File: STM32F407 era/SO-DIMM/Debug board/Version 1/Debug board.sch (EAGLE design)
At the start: 10 parts, among them J4 FTDI_DEVICE, X1 057-014-1, X2 BN35N61, X3 BN35N61, X4 BN35N61, X5 BN35N61, X6 BN35N61

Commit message: more work on debug board silkscreen
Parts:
- added J2, J3, J5, J6, J7: (no value), SparkFun-Connectors:BANANA_CONN
- R26: value 60 -> 120
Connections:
- net CANH renamed CAN_P
- net CANL renamed CAN_N
- net 12V: now also J5.1
- net 3.3V: now also J2.1
- net 5.0V: now also J3.1
- net GND: now also J6.1, J7.1
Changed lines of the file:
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@@
 <part name="GND7" library="supply1" deviceset="GND" device=""/>
 <part name="SW1" library="microbuilder" deviceset="SWITCH_DPDT" device=""/>
-<part name="R26" library="microbuilder" deviceset="RESISTOR" device="_0603" value="60"/>
+<part name="R26" library="microbuilder" deviceset="RESISTOR" device="_0603" value="120"/>
 <part name="X2" library="con-coax" deviceset="BN35N61" device=""/>
 <part name="X3" library="con-coax" deviceset="BN35N61" device=""/>
@@
 <part name="X5" library="con-coax" deviceset="BN35N61" device=""/>
 <part name="X6" library="con-coax" deviceset="BN35N61" device=""/>
+<part name="J2" library="SparkFun-Connectors" deviceset="BANANA_CONN" device=""/>
+<part name="J3" library="SparkFun-Connectors" deviceset="BANANA_CONN" device=""/>
+<part name="J5" library="SparkFun-Connectors" deviceset="BANANA_CONN" device=""/>
+<part name="J6" library="SparkFun-Connectors" deviceset="BANANA_CONN" device=""/>
+<part name="U$1" library="microbuilder" deviceset="3.3V" device=""/>
+<part name="U$2" library="microbuilder" deviceset="5.0V" device=""/>
+<part name="U$3" library="microbuilder" deviceset="12V" device=""/>
+<part name="GND9" library="supply1" deviceset="GND" device=""/>
+<part name="J7" library="SparkFun-Connectors" deviceset="BANANA_CONN" device=""/>
 </parts>
 <sheets>
@@
 <instance part="X5" gate="G$1" x="71.12" y="78.74" rot="MR0"/>
 <instance part="X6" gate="G$1" x="91.44" y="78.74" rot="MR0"/>
+<instance part="J2" gate="G$1" x="15.24" y="63.5"/>
+<instance part="J3" gate="G$1" x="15.24" y="58.42"/>
+<instance part="J5" gate="G$1" x="15.24" y="53.34"/>
+<instance part="J6" gate="G$1" x="15.24" y="48.26"/>
+<instance part="U$1" gate="G$1" x="10.16" y="68.58"/>
+<instance part="U$2" gate="G$1" x="5.08" y="68.58"/>
+<instance part="U$3" gate="G$1" x="0" y="68.58"/>
+<instance part="GND9" gate="1" x="10.16" y="40.64"/>
+<instance part="J7" gate="G$1" x="15.24" y="45.72"/>
 </instances>
 <busses>
@@
 <wire x1="55.88" y1="45.72" x2="55.88" y2="35.56" width="0.1524" layer="91"/>
 </segment>
+<segment>
+<pinref part="J6" gate="G$1" pin="1"/>
+<pinref part="GND9" gate="1" pin="GND"/>
+<wire x1="12.7" y1="48.26" x2="10.16" y2="48.26" width="0.1524" layer="91"/>
+<wire x1="10.16" y1="48.26" x2="10.16" y2="45.72" width="0.1524" layer="91"/>
+<pinref part="J7" gate="G$1" pin="1"/>
+<wire x1="10.16" y1="45.72" x2="10.16" y2="43.18" width="0.1524" layer="91"/>
+<wire x1="12.7" y1="45.72" x2="10.16" y2="45.72" width="0.1524" layer="91"/>
+<junction x="10.16" y="45.72"/>
+</segment>
 </net>
 <net name="3.3V" class="0">
@@
 <wire x1="5.08" y1="99.06" x2="5.08" y2="101.6" width="0.1524" layer="91"/>
 </segment>
+<segment>
+<pinref part="J2" gate="G$1" pin="1"/>
+<pinref part="U$1" gate="G$1" pin="3.3V"/>
+<wire x1="12.7" y1="63.5" x2="10.16" y2="63.5" width="0.1524" layer="91"/>
+<wire x1="10.16" y1="63.5" x2="10.16" y2="66.04" width="0.1524" layer="91"/>
+</segment>
 </net>
 <net name="12V" class="0">
@@
 <wire x1="-30.48" y1="96.52" x2="-30.48" y2="101.6" width="0.1524" layer="91"/>
 </segment>
-</net>
-<net name="CANH" class="0">
+<segment>
+<pinref part="J5" gate="G$1" pin="1"/>
+<pinref part="U$3" gate="G$1" pin="12V"/>
+<wire x1="12.7" y1="53.34" x2="0" y2="53.34" width="0.1524" layer="91"/>
+<wire x1="0" y1="53.34" x2="0" y2="66.04" width="0.1524" layer="91"/>
+</segment>
+</net>
+<net name="CAN_P" class="0">
 <segment>
 <pinref part="X1" gate="-7" pin="S"/>
@@
 </segment>
 </net>
-<net name="CANL" class="0">
+<net name="CAN_N" class="0">
 <segment>
 <pinref part="X1" gate="-8" pin="S"/>
@@
 <wire x1="-25.4" y1="99.06" x2="-25.4" y2="101.6" width="0.1524" layer="91"/>
 </segment>
-</net>
+<segment>
+<pinref part="J3" gate="G$1" pin="1"/>
+<pinref part="U$2" gate="G$1" pin="5.0V"/>
+<wire x1="12.7" y1="58.42" x2="5.08" y2="58.42" width="0.1524" layer="91"/>
+<wire x1="5.08" y1="58.42" x2="5.08" y2="66.04" width="0.1524" layer="91"/>
+</segment>
+</net>

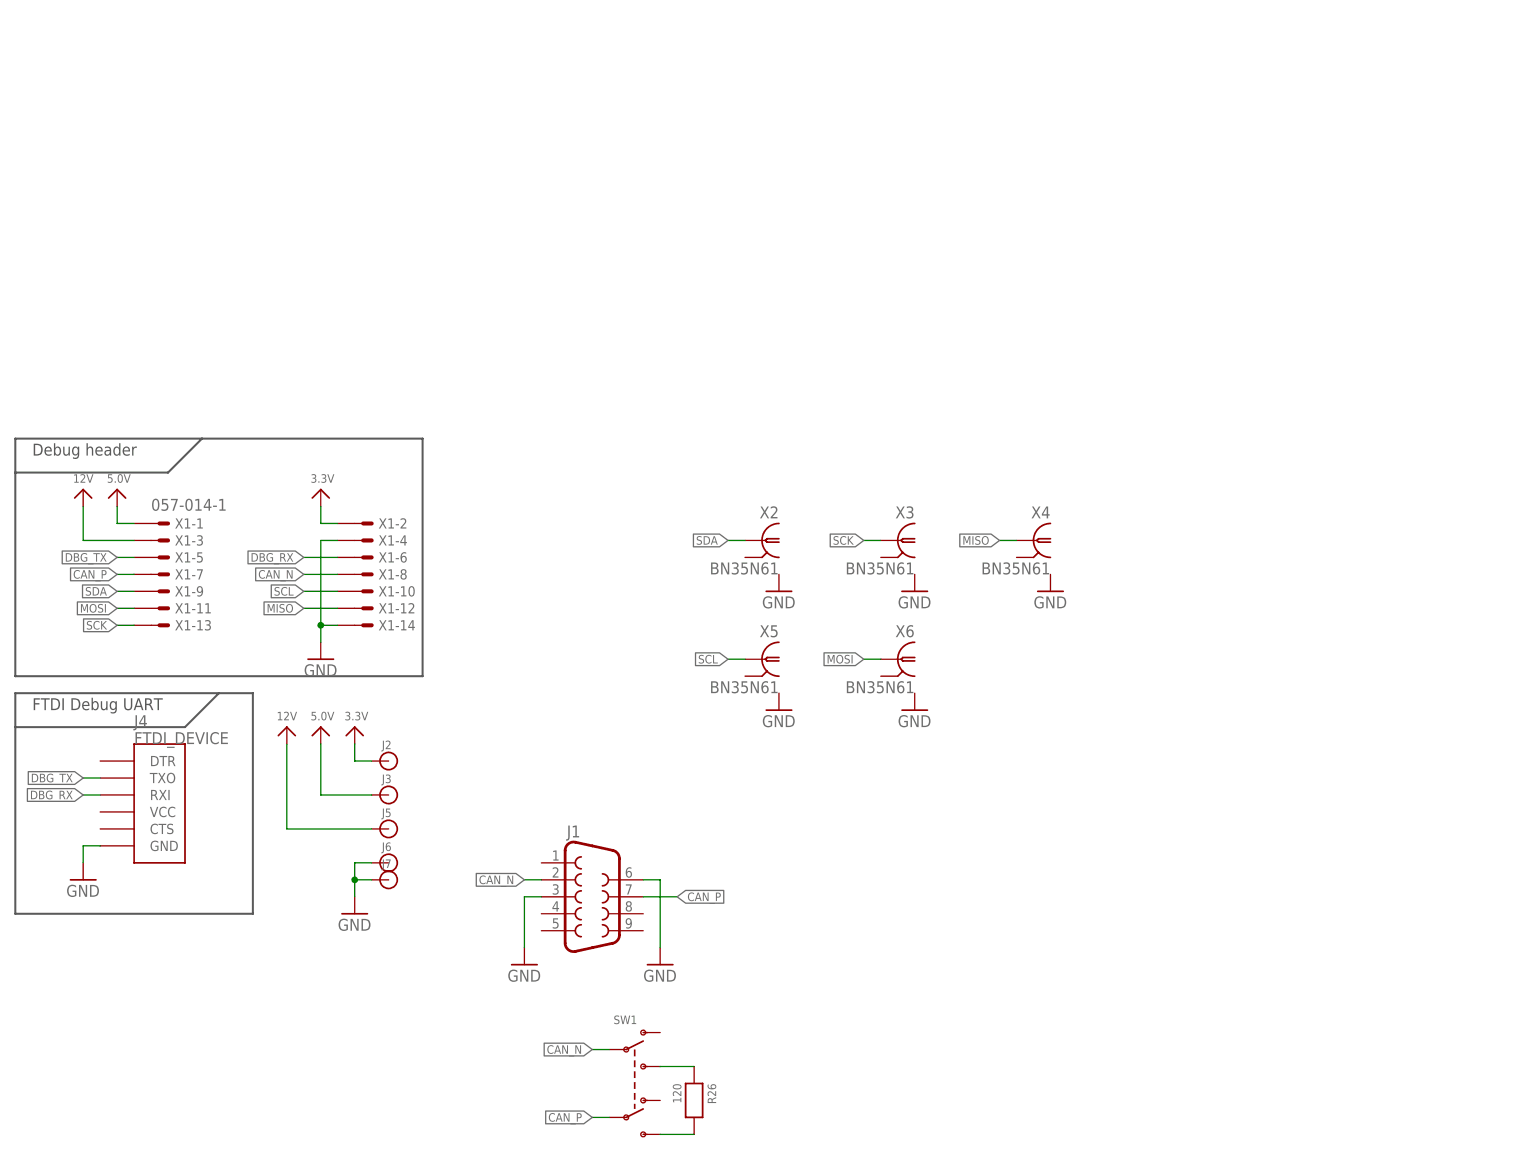
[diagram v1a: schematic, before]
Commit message: added 12V aux power to debug board
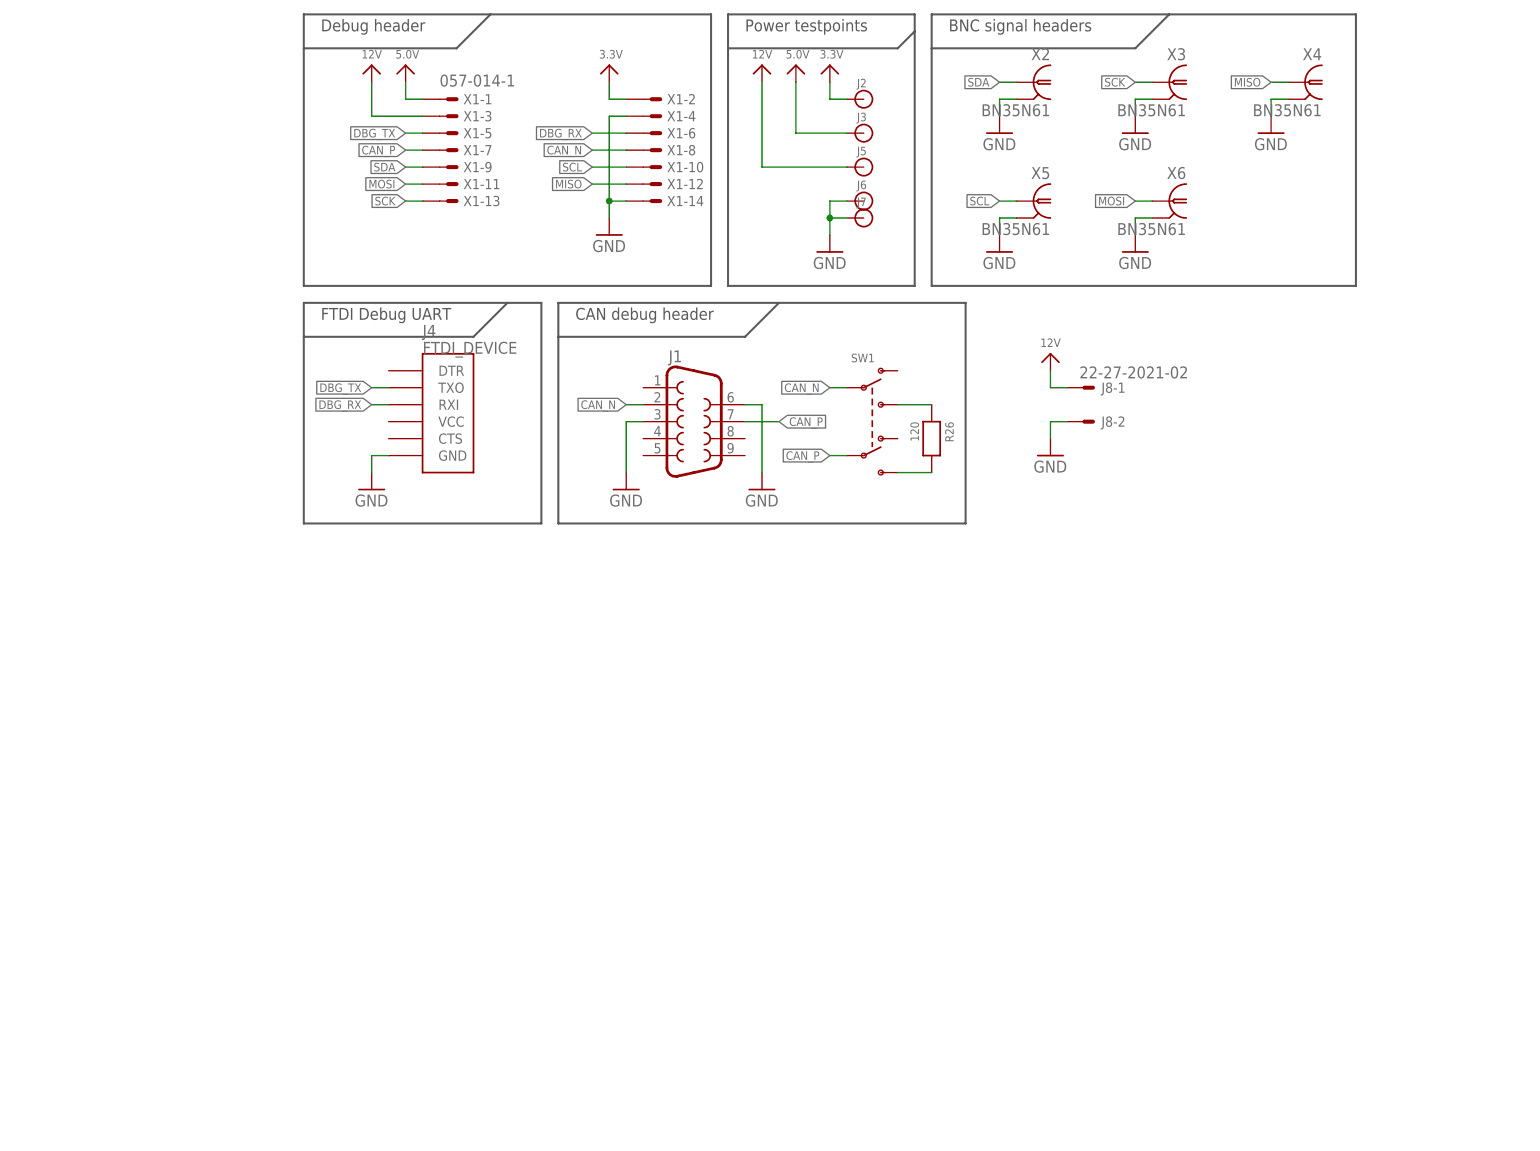
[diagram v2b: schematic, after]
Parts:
- added J8: 22-27-2021-02, con-molex:22-27-2021-02
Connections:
- net 12V: now also J8-1.S
- net GND: now also J8-2.S, X2G$1.GND, X3G$1.GND, X4G$1.GND, X5G$1.GND, X6G$1.GND
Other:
- note added: "BNC signal headers"
- note added: "CAN debug header"
- note added: "Power testpoints"
- moved on the sheet: J1, J2, J3, J4, J5, J6, J7, R26, SW1, X1-1, X1-10, X1-11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

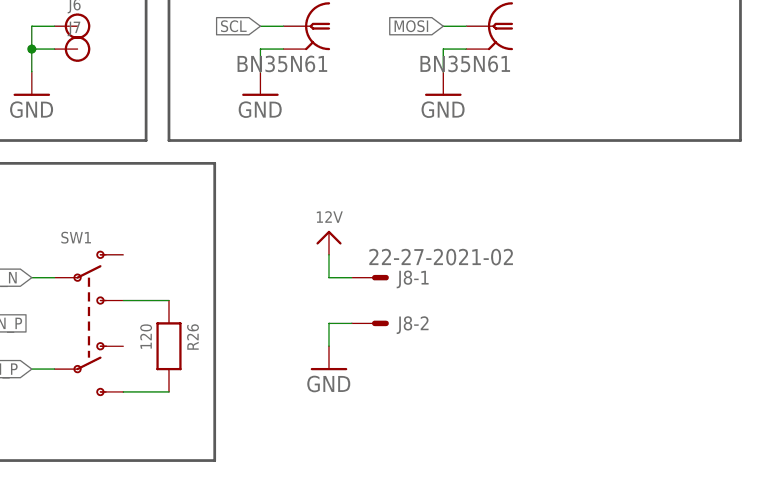
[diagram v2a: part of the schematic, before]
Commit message: USB to UART done, mork work on COM/TC
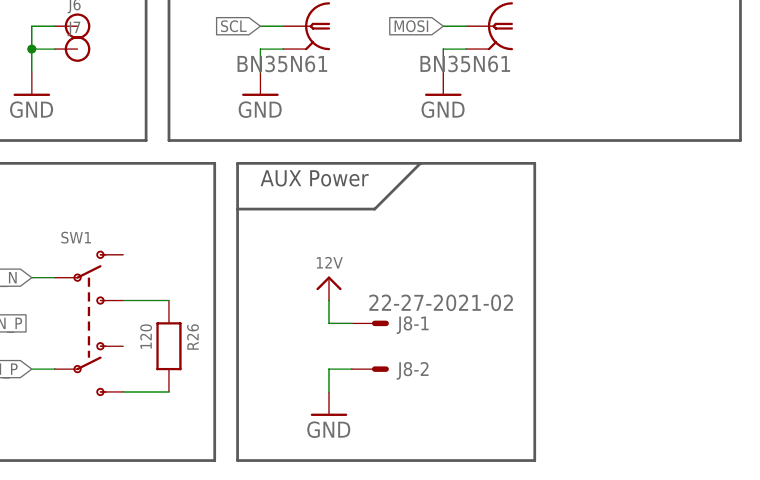
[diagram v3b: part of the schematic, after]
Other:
- note added: "AUX Power"
- moved on the sheet: J8-1, J8-2
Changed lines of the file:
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@@
 <wire x1="96.52" y1="170.18" x2="127" y2="170.18" width="0.3048" layer="97"/>
 <wire x1="127" y1="170.18" x2="132.08" y2="175.26" width="0.3048" layer="97"/>
+<wire x1="104.14" y1="132.08" x2="124.46" y2="132.08" width="0.3048" layer="97"/>
+<wire x1="124.46" y1="132.08" x2="137.16" y2="132.08" width="0.3048" layer="97"/>
+<wire x1="137.16" y1="132.08" x2="137.16" y2="99.06" width="0.3048" layer="97"/>
+<wire x1="137.16" y1="99.06" x2="104.14" y2="99.06" width="0.3048" layer="97"/>
+<wire x1="104.14" y1="99.06" x2="104.14" y2="127" width="0.3048" layer="97"/>
+<text x="106.68" y="129.54" size="1.778" layer="97" font="vector">AUX Power</text>
+<wire x1="104.14" y1="127" x2="104.14" y2="132.08" width="0.3048" layer="97"/>
+<wire x1="104.14" y1="127" x2="119.38" y2="127" width="0.3048" layer="97"/>
+<wire x1="119.38" y1="127" x2="124.46" y2="132.08" width="0.3048" layer="97"/>
 </plain>
 <instances>
@@
 <instance part="J7" gate="G$1" x="86.36" y="144.78"/>
 <instance part="FRAME1" gate="G$1" x="0" y="0"/>
-<instance part="J8" gate="-1" x="119.38" y="119.38"/>
-<instance part="J8" gate="-2" x="119.38" y="114.3"/>
-<instance part="U$4" gate="G$1" x="114.3" y="124.46"/>
-<instance part="GND10" gate="1" x="114.3" y="109.22"/>
+<instance part="J8" gate="-1" x="119.38" y="114.3"/>
+<instance part="J8" gate="-2" x="119.38" y="109.22"/>
+<instance part="U$4" gate="G$1" x="114.3" y="119.38"/>
+<instance part="GND10" gate="1" x="114.3" y="104.14"/>
 </instances>
 <busses>
@@
 <pinref part="J8" gate="-2" pin="S"/>
 <pinref part="GND10" gate="1" pin="GND"/>
-<wire x1="116.84" y1="114.3" x2="114.3" y2="114.3" width="0.1524" layer="91"/>
-<wire x1="114.3" y1="114.3" x2="114.3" y2="111.76" width="0.1524" layer="91"/>
+<wire x1="116.84" y1="109.22" x2="114.3" y2="109.22" width="0.1524" layer="91"/>
+<wire x1="114.3" y1="109.22" x2="114.3" y2="106.68" width="0.1524" layer="91"/>
 </segment>
 </net>
@@
 <pinref part="J8" gate="-1" pin="S"/>
 <pinref part="U$4" gate="G$1" pin="12V"/>
-<wire x1="116.84" y1="119.38" x2="114.3" y2="119.38" width="0.1524" layer="91"/>
-<wire x1="114.3" y1="119.38" x2="114.3" y2="121.92" width="0.1524" layer="91"/>
+<wire x1="116.84" y1="114.3" x2="114.3" y2="114.3" width="0.1524" layer="91"/>
+<wire x1="114.3" y1="114.3" x2="114.3" y2="116.84" width="0.1524" layer="91"/>
 </segment>
 </net>
